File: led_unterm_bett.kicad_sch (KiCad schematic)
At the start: 27 parts, among them J1 Conn_01x03, J2 Conn_01x03, J3 Conn_01x03, J4 Conn_01x02, J5 Screw_Terminal_01x02, J6 Conn_01x04, Q1 BSS138, Q2 BSS138, Q3 BSS138, U1 NodeMCU1.0(ESP-12E), U2 LM7805_TO220

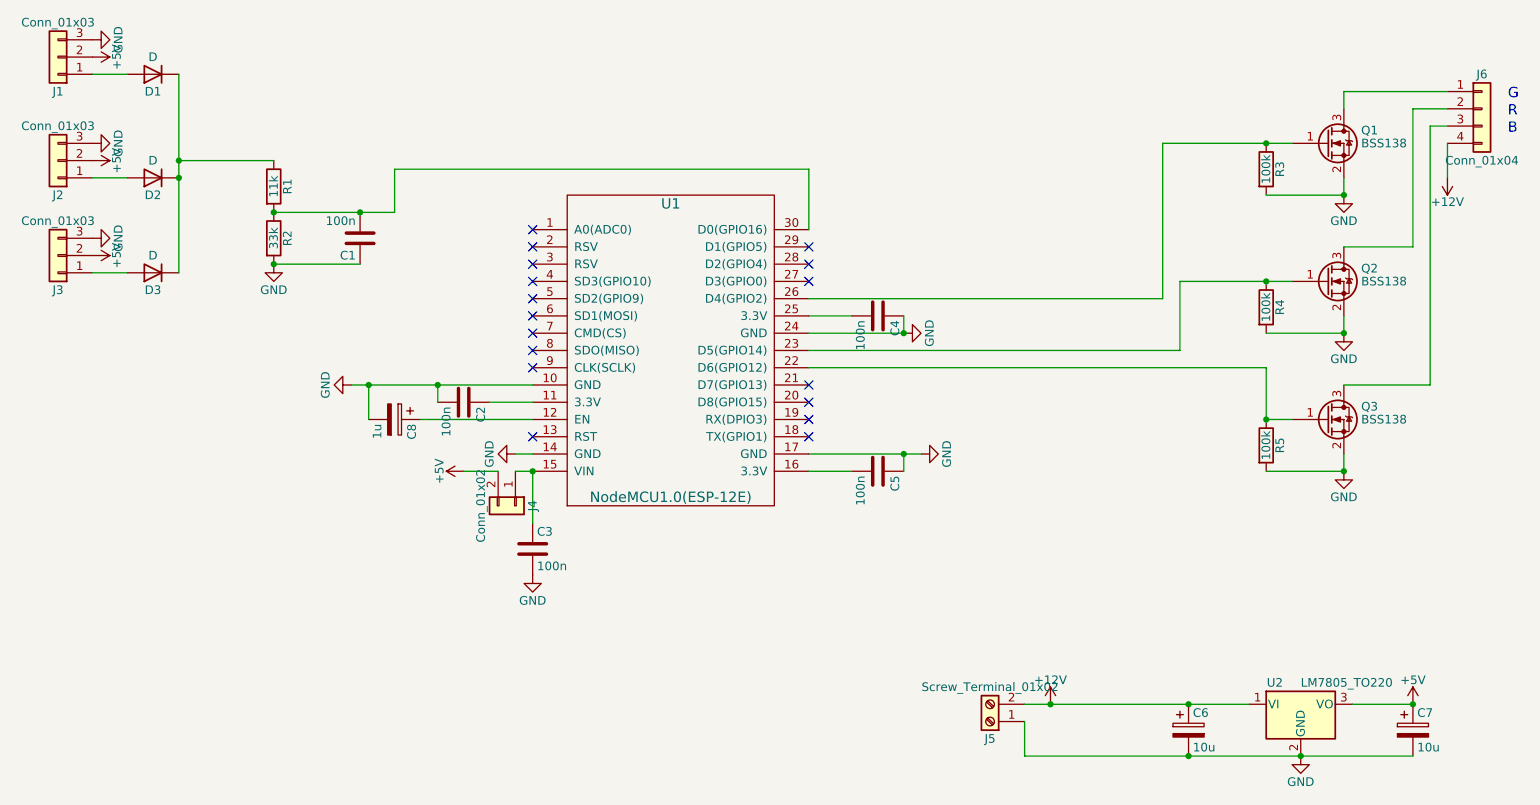
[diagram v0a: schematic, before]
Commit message: update some resistor values
so the 0805er E-series set lasts longer ;-)
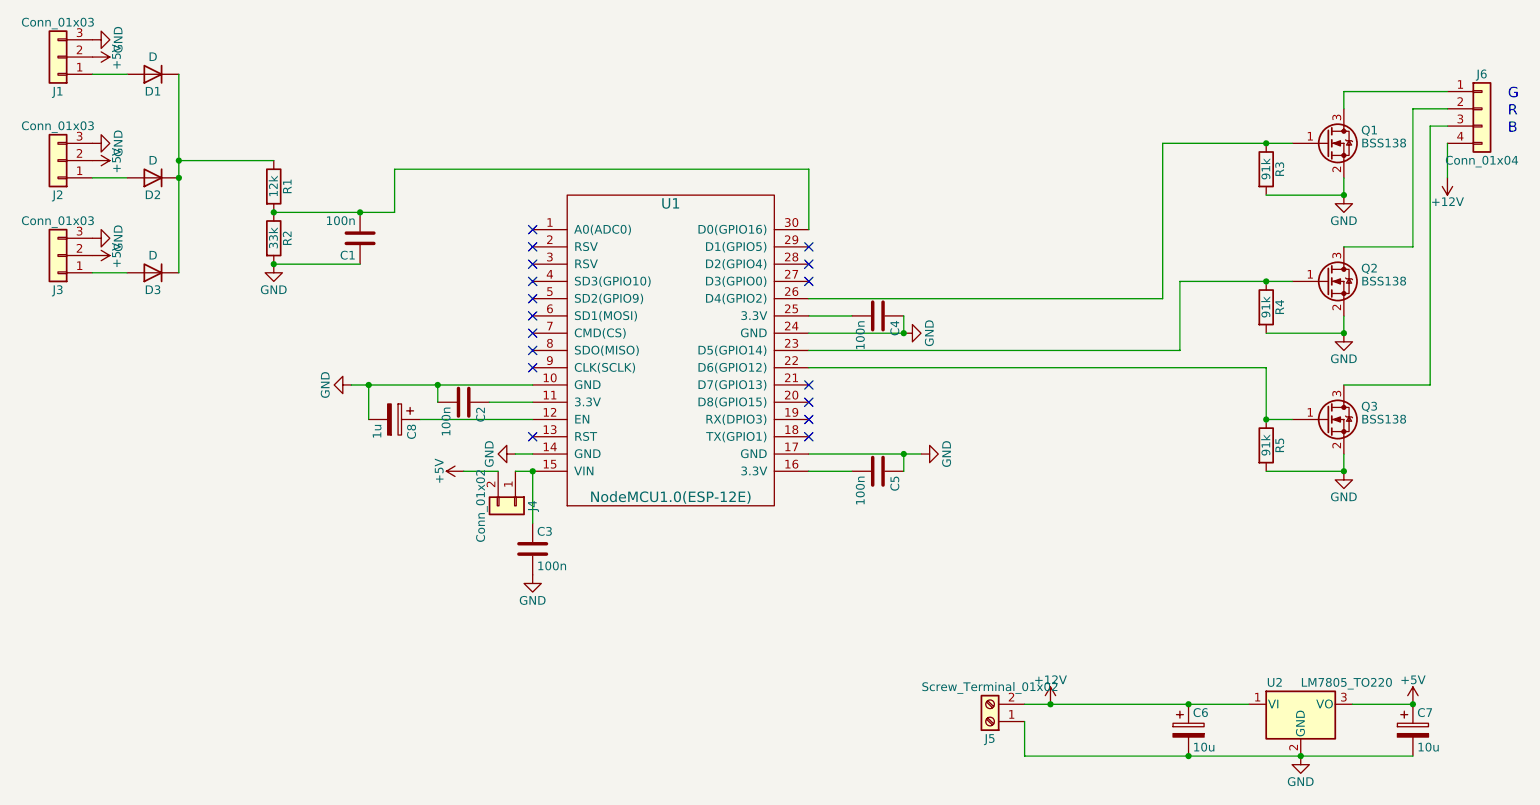
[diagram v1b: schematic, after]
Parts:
- R1: value 11k -> 12k
- R3, R4, R5: value 100k -> 91k
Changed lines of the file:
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@@
     (in_bom yes) (on_board yes)
     (property "Reference" "R3" (id 0) (at 212.852 35.56 90))
-    (property "Value" "100k" (id 1) (at 210.82 35.56 90))
+    (property "Value" "91k" (id 1) (at 210.82 35.56 90))
     (property "Footprint" "Resistors_SMD:R_0805_HandSoldering" (id 2) (at 209.042 35.56 90)
       (effects (font (size 1.27 1.27)) hide)
@@
     (in_bom yes) (on_board yes)
     (property "Reference" "R4" (id 0) (at 212.852 55.88 90))
-    (property "Value" "100k" (id 1) (at 210.82 55.88 90))
+    (property "Value" "91k" (id 1) (at 210.82 55.88 90))
     (property "Footprint" "Resistors_SMD:R_0805_HandSoldering" (id 2) (at 209.042 55.88 90)
       (effects (font (size 1.27 1.27)) hide)
@@
     (in_bom yes) (on_board yes)
     (property "Reference" "R5" (id 0) (at 212.852 76.2 90))
-    (property "Value" "100k" (id 1) (at 210.82 76.2 90))
+    (property "Value" "91k" (id 1) (at 210.82 76.2 90))
     (property "Footprint" "Resistors_SMD:R_0805_HandSoldering" (id 2) (at 209.042 76.2 90)
       (effects (font (size 1.27 1.27)) hide)
@@
     (in_bom yes) (on_board yes)
     (property "Reference" "R1" (id 0) (at 66.802 38.1 90))
-    (property "Value" "11k" (id 1) (at 64.77 38.1 90))
+    (property "Value" "12k" (id 1) (at 64.77 38.1 90))
     (property "Footprint" "Resistors_SMD:R_0805_HandSoldering" (id 2) (at 62.992 38.1 90)
       (effects (font (size 1.27 1.27)) hide)
@@
     )
     (path "/00000000-0000-0000-0000-00005f563b4a"
-      (reference "R1") (unit 1) (value "11k") (footprint "Resistors_SMD:R_0805_HandSoldering")
+      (reference "R1") (unit 1) (value "12k") (footprint "Resistors_SMD:R_0805_HandSoldering")
     )
     (path "/00000000-0000-0000-0000-00005f563bc3"
@@
     )
     (path "/00000000-0000-0000-0000-00005f550bb7"
-      (reference "R3") (unit 1) (value "100k") (footprint "Resistors_SMD:R_0805_HandSoldering")
+      (reference "R3") (unit 1) (value "91k") (footprint "Resistors_SMD:R_0805_HandSoldering")
     )
     (path "/00000000-0000-0000-0000-00005f550e35"
-      (reference "R4") (unit 1) (value "100k") (footprint "Resistors_SMD:R_0805_HandSoldering")
+      (reference "R4") (unit 1) (value "91k") (footprint "Resistors_SMD:R_0805_HandSoldering")
     )
     (path "/00000000-0000-0000-0000-00005f550f95"
-      (reference "R5") (unit 1) (value "100k") (footprint "Resistors_SMD:R_0805_HandSoldering")
+      (reference "R5") (unit 1) (value "91k") (footprint "Resistors_SMD:R_0805_HandSoldering")
     )
     (path "/00000000-0000-0000-0000-00005f55090f"
